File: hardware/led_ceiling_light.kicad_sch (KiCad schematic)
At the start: 22 parts, among them J1 Screw_Terminal_01x03, Q1 BSS123, U1 AL8861

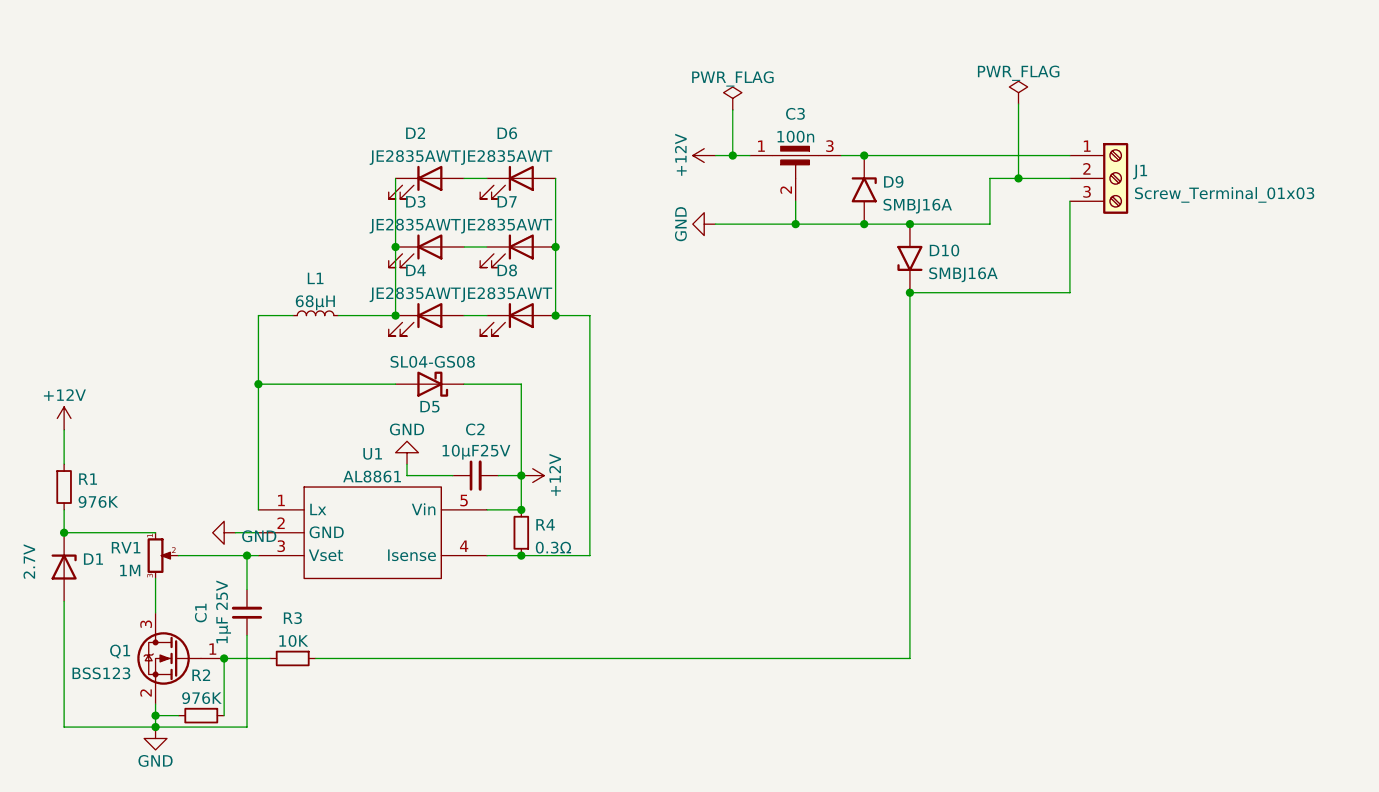
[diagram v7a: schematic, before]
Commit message: Add optional a 3rd LED in serie (so we can have a 3x2 or 3x3 matrix). Re-annotate whole schematic
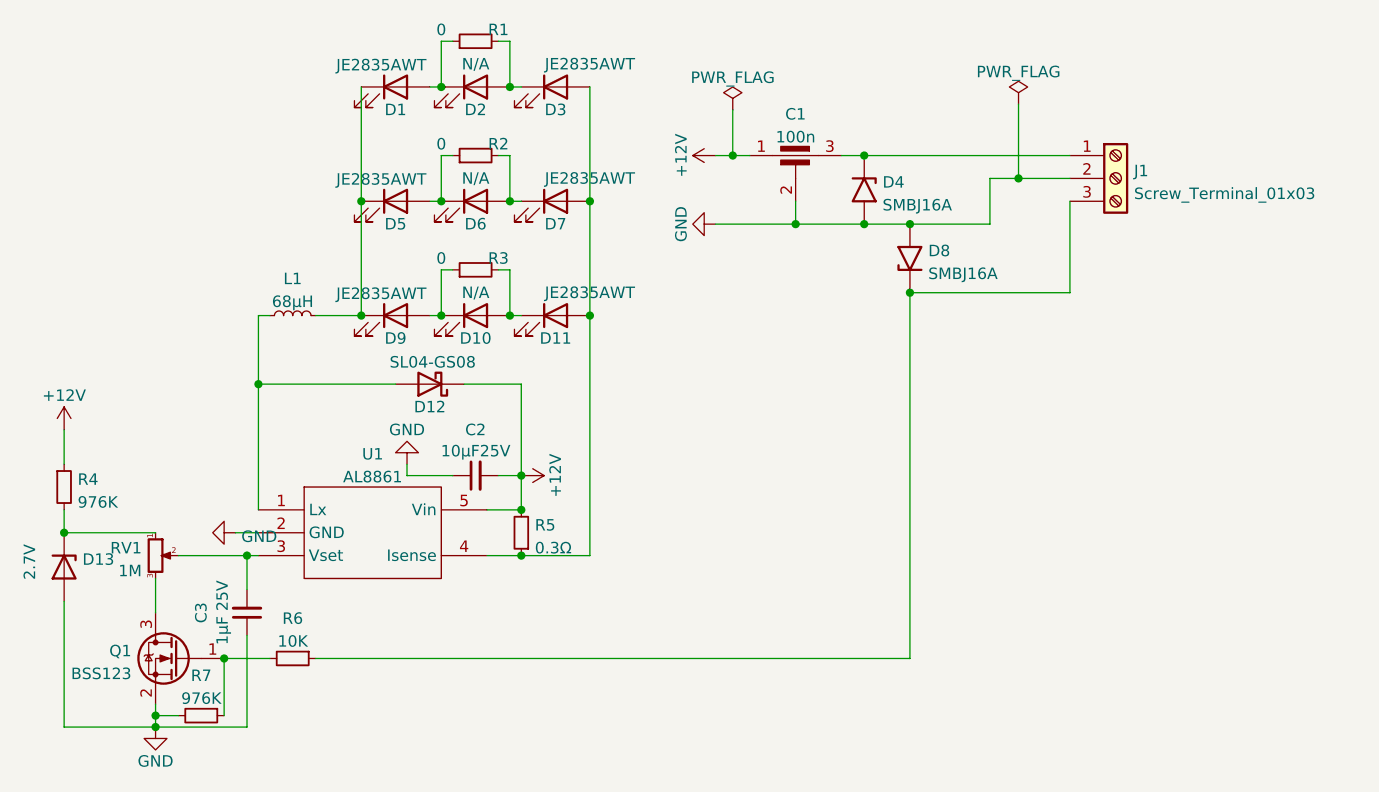
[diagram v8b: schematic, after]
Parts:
- added D10, D2, D6: N/A, LED_SMD:LED_PLCC_2835_Handsoldering, symbol Device:LED
- added R1, R2, R3: 0, Resistor_THT:R_Axial_DIN0204_L3.6mm_D1.6mm_P7.62mm_Horizontal, symbol Device:R_Small
- renumbered C3 to C1, C1 to C3, D2 to D1, D8 to D11, D5 to D12, D1 to D13, D6 to D3, D9 to D4, D3 to D5, D10 to D8, D4 to D9, R1 to R4, R4 to R5, R3 to R6, R2 to R7
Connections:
- net at D1.2 (A): now also D2.1 (K), R1.1; no longer D3.1 (K)
- net at D9.2 (A): now also D10.1 (K), R3.1; no longer D11.1 (K)
- net at D5.2 (A): now also D6.1 (K), R2.1; no longer D7.1 (K)
- new net: D2.2 (A), D3.1 (K), R1.2
- new net: D10.2 (A), D11.1 (K), R3.2
- new net: D6.2 (A), D7.1 (K), R2.2
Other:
- moved on the sheet: D1, D11, D3, D5, D7, D9, L1
